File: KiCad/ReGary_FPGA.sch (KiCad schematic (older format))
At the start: 28 parts, among them J1 Conn_01x02, U1 GW1N-UV1P5LQ100, U2 LM1117-3.3, U3 TPS73643DBV

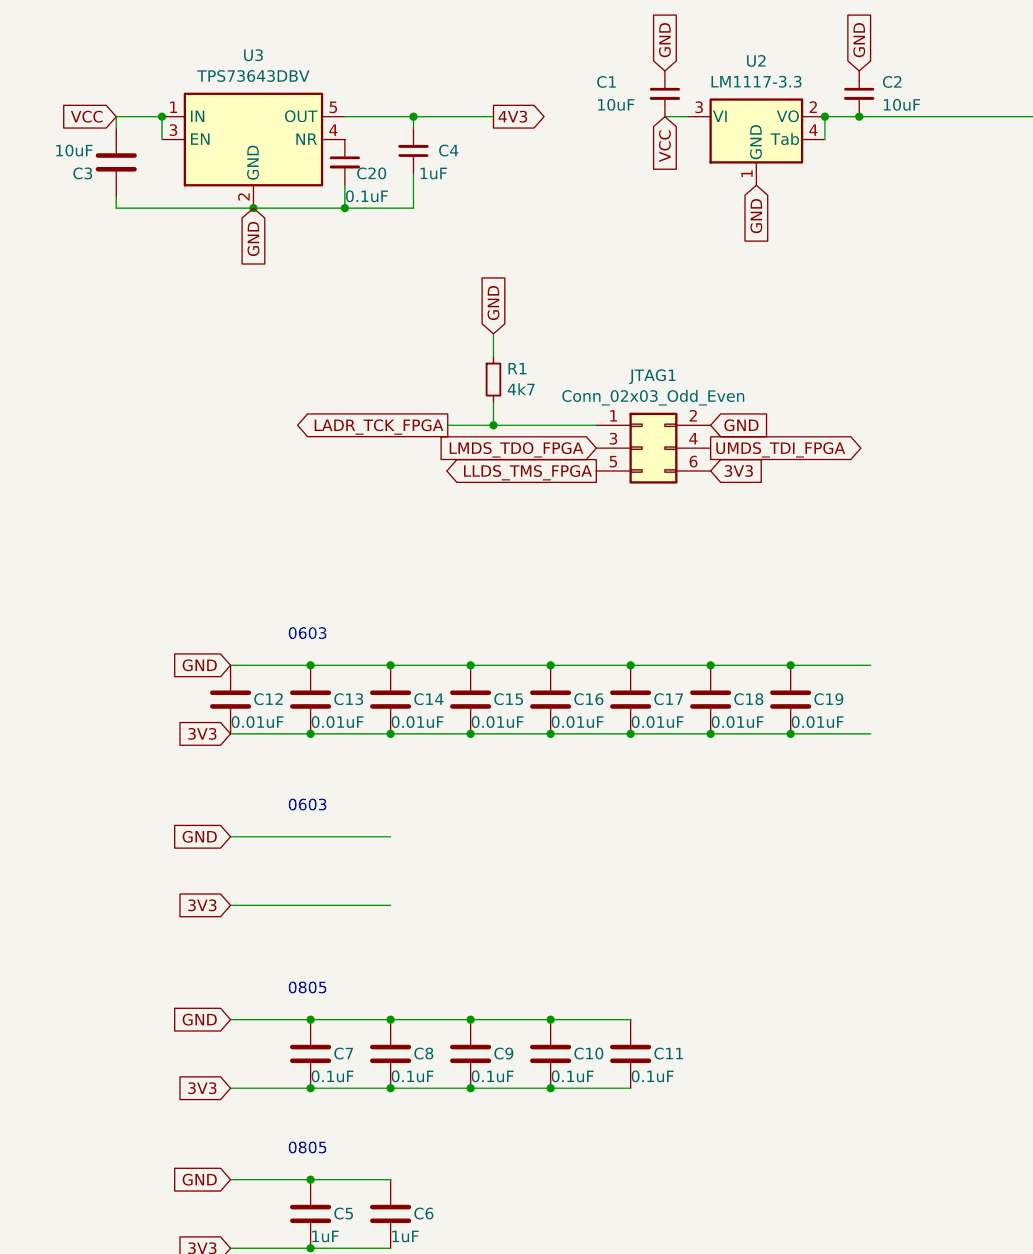
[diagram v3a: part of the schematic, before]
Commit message: Fixed enumeration of capacitors and placement of last capacitor C11 for 3V3-power
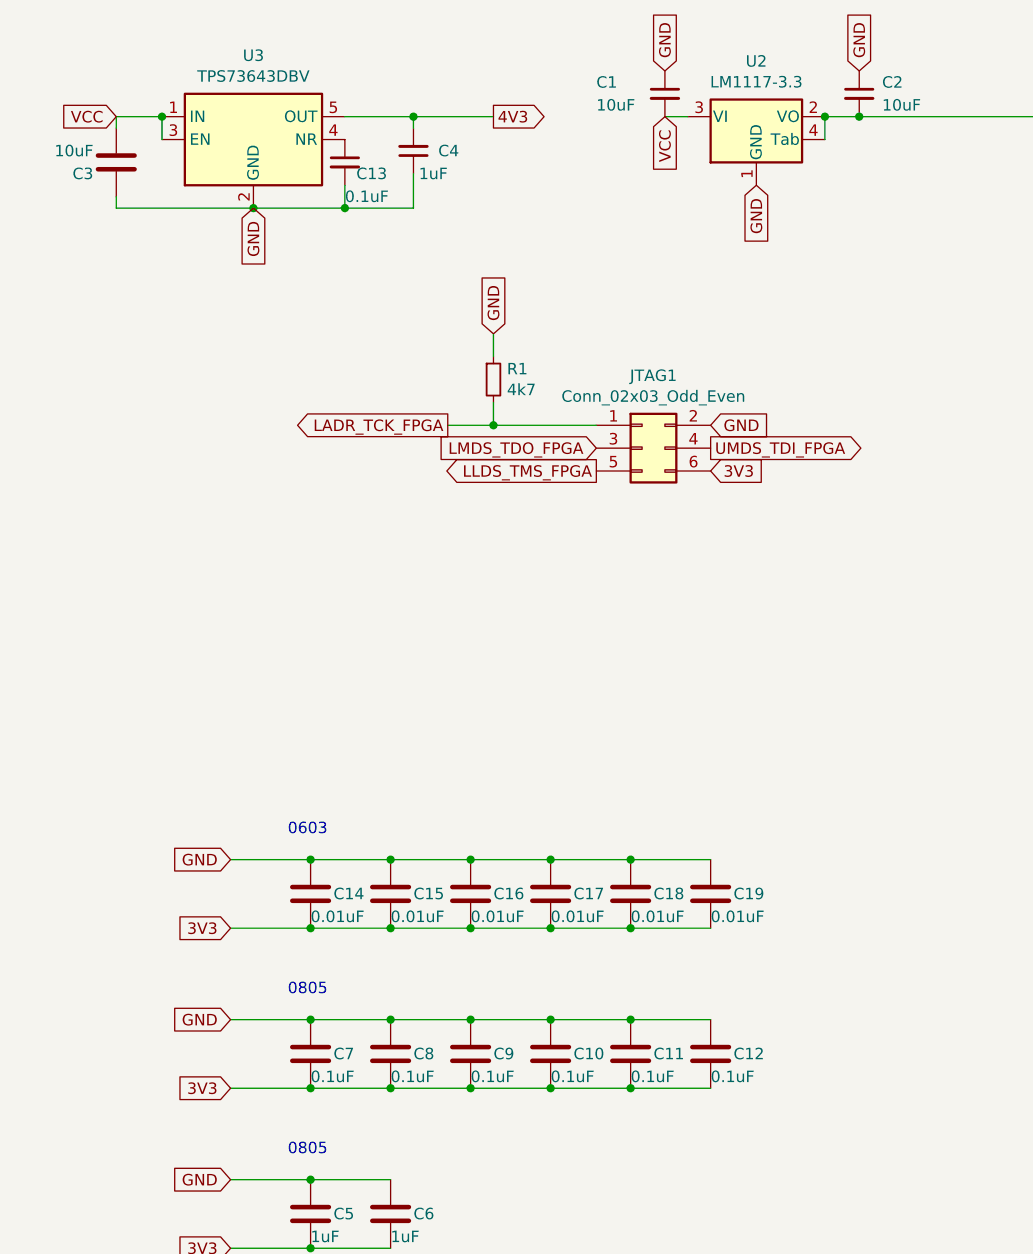
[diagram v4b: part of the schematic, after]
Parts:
- removed C19: 0.01uF, Capacitor_SMD:C_0603_1608Metric_Pad1.08x0.95mm_HandSolder, symbol Device:C
- C11: renamed from C18; value 0.01uF -> 0.1uF; footprint Capacitor_SMD:C_0603_1608Metric_Pad1.08x0.95mm_HandSolder -> Capacitor_SMD:C_0805_2012Metric_Pad1.18x1.45mm_HandSolder
- renumbered C11 to C12, C20 to C13, C12 to C14, C13 to C15, C14 to C16, C15 to C17, C16 to C18, C17 to C19
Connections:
- wire segments 78 -> 74
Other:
- moved on the sheet: C11, C12, C14, C15, C16, C17, C18, C19
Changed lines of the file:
@@
 Text GLabel 8400 2150 1    50   Input ~ 0
 GND
-Text GLabel 7250 3600 0    50   Input ~ 0
-GND
-$Comp
-L Device:C C?
-U 1 1 60CC8EFC
-P 9700 3750
-AR Path="/60CC8EFC" Ref="C?"  Part="1"
-AR Path="/608A10F5/60CC8EFC" Ref="C19"  Part="1"
-F 0 "C19" H 9800 3750 50  0000 L CNN
-F 1 "0.01uF" H 9700 3650 50  0000 L CNN
-F 2 "Capacitor_SMD:C_0603_1608Metric_Pad1.08x0.95mm_HandSolder" H 9738 3600 50  0001 C CNN
-F 3 "~" H 9700 3750 50  0001 C CNN
-	1    9700 3750
-	1    0    0    -1
-$EndComp
+Text GLabel 7250 4450 0    50   Input ~ 0
+GND
 $Comp
 L Device:C C?
 U 1 1 60CC8F02
-P 9350 3750
+P 9000 5300
 AR Path="/60CC8F02" Ref="C?"  Part="1"
-AR Path="/608A10F5/60CC8F02" Ref="C18"  Part="1"
-F 0 "C18" H 9450 3750 50  0000 L CNN
-F 1 "0.01uF" H 9350 3650 50  0000 L CNN
-F 2 "Capacitor_SMD:C_0603_1608Metric_Pad1.08x0.95mm_HandSolder" H 9388 3600 50  0001 C CNN
-F 3 "~" H 9350 3750 50  0001 C CNN
-	1    9350 3750
-	1    0    0    -1
-$EndComp
-Connection ~ 7600 3600
-Wire Wire Line
-	7600 3600 7950 3600
-Connection ~ 7600 3900
-Wire Wire Line
-	7600 3900 7950 3900
+AR Path="/608A10F5/60CC8F02" Ref="C11"  Part="1"
+F 0 "C11" H 9100 5300 50  0000 L CNN
+F 1 "0.1uF" H 9000 5200 50  0000 L CNN
+F 2 "Capacitor_SMD:C_0805_2012Metric_Pad1.18x1.45mm_HandSolder" H 9038 5150 50  0001 C CNN
+F 3 "~" H 9000 5300 50  0001 C CNN
+	1    9000 5300
+	1    0    0    -1
+$EndComp
+Connection ~ 7600 4450
+Wire Wire Line
+	7600 4450 7950 4450
+Connection ~ 7600 4750
+Wire Wire Line
+	7600 4750 7950 4750
 $Comp
 L Device:C C?
@@
 	1    0    0    -1
 $EndComp
-Connection ~ 7950 3600
-Connection ~ 7950 3900
-Wire Wire Line
-	7950 3600 8300 3600
-Wire Wire Line
-	7950 3900 8300 3900
+Connection ~ 7950 4450
+Connection ~ 7950 4750
+Wire Wire Line
+	7950 4450 8300 4450
+Wire Wire Line
+	7950 4750 8300 4750
 Text GLabel 7250 5450 0    50   Input ~ 0
 3V3
-Connection ~ 8300 3600
-Wire Wire Line
-	9000 3900 9350 3900
+Connection ~ 8300 4450
+Wire Wire Line
+	9000 4750 9350 4750
 $Comp
 L Device:C C?
@@
 	1    0    0    -1
 $EndComp
-Wire Wire Line
-	9700 3900 9350 3900
-Connection ~ 9350 3900
 $Comp
 L Device:R_Pack04 RN1
@@
 L Device:C C?
 U 1 1 60636E2E
-P 7250 3750
+P 7600 4600
 AR Path="/60636E2E" Ref="C?"  Part="1"
-AR Path="/608A10F5/60636E2E" Ref="C12"  Part="1"
-F 0 "C12" H 7350 3750 50  0000 L CNN
-F 1 "0.01uF" H 7250 3650 50  0000 L CNN
-F 2 "Capacitor_SMD:C_0603_1608Metric_Pad1.08x0.95mm_HandSolder" H 7288 3600 50  0001 C CNN
-F 3 "~" H 7250 3750 50  0001 C CNN
-	1    7250 3750
+AR Path="/608A10F5/60636E2E" Ref="C14"  Part="1"
+F 0 "C14" H 7700 4600 50  0000 L CNN
+F 1 "0.01uF" H 7600 4500 50  0000 L CNN
+F 2 "Capacitor_SMD:C_0603_1608Metric_Pad1.08x0.95mm_HandSolder" H 7638 4450 50  0001 C CNN
+F 3 "~" H 7600 4600 50  0001 C CNN
+	1    7600 4600
 	1    0    0    -1
 $EndComp
@@
 L Device:C C?
 U 1 1 60637476
-P 7600 3750
+P 7950 4600
 AR Path="/60637476" Ref="C?"  Part="1"
-AR Path="/608A10F5/60637476" Ref="C13"  Part="1"
-F 0 "C13" H 7700 3750 50  0000 L CNN
-F 1 "0.01uF" H 7600 3650 50  0000 L CNN
-F 2 "Capacitor_SMD:C_0603_1608Metric_Pad1.08x0.95mm_HandSolder" H 7638 3600 50  0001 C CNN
-F 3 "~" H 7600 3750 50  0001 C CNN
-	1    7600 3750
+AR Path="/608A10F5/60637476" Ref="C15"  Part="1"
+F 0 "C15" H 8050 4600 50  0000 L CNN
+F 1 "0.01uF" H 7950 4500 50  0000 L CNN
+F 2 "Capacitor_SMD:C_0603_1608Metric_Pad1.08x0.95mm_HandSolder" H 7988 4450 50  0001 C CNN
+F 3 "~" H 7950 4600 50  0001 C CNN
+	1    7950 4600
 	1    0    0    -1
 $EndComp
@@
 L Device:C C?
 U 1 1 60637B30
-P 8300 3750
+P 8650 4600
 AR Path="/60637B30" Ref="C?"  Part="1"
-AR Path="/608A10F5/60637B30" Ref="C15"  Part="1"
-F 0 "C15" H 8400 3750 50  0000 L CNN
-F 1 "0.01uF" H 8300 3650 50  0000 L CNN
-F 2 "Capacitor_SMD:C_0603_1608Metric_Pad1.08x0.95mm_HandSolder" H 8338 3600 50  0001 C CNN
-F 3 "~" H 8300 3750 50  0001 C CNN
-	1    8300 3750
+AR Path="/608A10F5/60637B30" Ref="C17"  Part="1"
+F 0 "C17" H 8750 4600 50  0000 L CNN
+F 1 "0.01uF" H 8650 4500 50  0000 L CNN
+F 2 "Capacitor_SMD:C_0603_1608Metric_Pad1.08x0.95mm_HandSolder" H 8688 4450 50  0001 C CNN
+F 3 "~" H 8650 4600 50  0001 C CNN
+	1    8650 4600
 	1    0    0    -1
 $EndComp
@@
 L Device:C C?
 U 1 1 60638427
-P 8650 3750
+P 9000 4600
 AR Path="/60638427" Ref="C?"  Part="1"
-AR Path="/608A10F5/60638427" Ref="C16"  Part="1"
-F 0 "C16" H 8750 3750 50  0000 L CNN
-F 1 "0.01uF" H 8650 3650 50  0000 L CNN
-F 2 "Capacitor_SMD:C_0603_1608Metric_Pad1.08x0.95mm_HandSolder" H 8688 3600 50  0001 C CNN
-F 3 "~" H 8650 3750 50  0001 C CNN
-	1    8650 3750
-	1    0    0    -1
-$EndComp
-Wire Wire Line
-	9700 3900 10050 3900
-Connection ~ 9700 3900
-Wire Wire Line
-	7250 3900 7600 3900
-Wire Wire Line
-	7250 3600 7600 3600
+AR Path="/608A10F5/60638427" Ref="C18"  Part="1"
+F 0 "C18" H 9100 4600 50  0000 L CNN
+F 1 "0.01uF" H 9000 4500 50  0000 L CNN
+F 2 "Capacitor_SMD:C_0603_1608Metric_Pad1.08x0.95mm_HandSolder" H 9038 4450 50  0001 C CNN
+F 3 "~" H 9000 4600 50  0001 C CNN
+	1    9000 4600
+	1    0    0    -1
+$EndComp
+Wire Wire Line
+	7250 4750 7600 4750
+Wire Wire Line
+	7250 4450 7600 4450
 Text GLabel 7250 5150 0    50   Input ~ 0
 GND
-Text GLabel 7250 3900 0    50   Input ~ 0
-3V3
-Text Notes 7500 3500 0    50   ~ 0
+Text GLabel 7250 4750 0    50   Input ~ 0
+3V3
+Text Notes 7500 4350 0    50   ~ 0
 0603
 Text Notes 7500 5050 0    50   ~ 0
@@
 L Device:C C?
 U 1 1 60898D1D
-P 9000 3750
+P 9350 4600
 AR Path="/60898D1D" Ref="C?"  Part="1"
-AR Path="/608A10F5/60898D1D" Ref="C17"  Part="1"
-F 0 "C17" H 9100 3750 50  0000 L CNN
-F 1 "0.01uF" H 9000 3650 50  0000 L CNN
-F 2 "Capacitor_SMD:C_0603_1608Metric_Pad1.08x0.95mm_HandSolder" H 9038 3600 50  0001 C CNN
-F 3 "~" H 9000 3750 50  0001 C CNN
-	1    9000 3750
-	1    0    0    -1
-$EndComp
-Wire Wire Line
-	9350 3600 9700 3600
-Connection ~ 9350 3600
-Wire Wire Line
-	8300 3600 8650 3600
-Connection ~ 8650 3600
-Wire Wire Line
-	8650 3600 9000 3600
+AR Path="/608A10F5/60898D1D" Ref="C19"  Part="1"
+F 0 "C19" H 9450 4600 50  0000 L CNN
+F 1 "0.01uF" H 9350 4500 50  0000 L CNN
+F 2 "Capacitor_SMD:C_0603_1608Metric_Pad1.08x0.95mm_HandSolder" H 9388 4450 50  0001 C CNN
+F 3 "~" H 9350 4600 50  0001 C CNN
+	1    9350 4600
+	1    0    0    -1
+$EndComp
+Wire Wire Line
+	8300 4450 8650 4450
+Connection ~ 8650 4450
+Wire Wire Line
+	8650 4450 9000 4450
 $Comp
 L Device:C C?
 U 1 1 608A7236
-P 7950 3750
+P 8300 4600
 AR Path="/608A7236" Ref="C?"  Part="1"
-AR Path="/608A10F5/608A7236" Ref="C14"  Part="1"
-F 0 "C14" H 8050 3750 50  0000 L CNN
-F 1 "0.01uF" H 7950 3650 50  0000 L CNN
-F 2 "Capacitor_SMD:C_0603_1608Metric_Pad1.08x0.95mm_HandSolder" H 7988 3600 50  0001 C CNN
-F 3 "~" H 7950 3750 50  0001 C CNN
-	1    7950 3750
-	1    0    0    -1
-$EndComp
-Connection ~ 9000 3600
-Wire Wire Line
-	9000 3600 9350 3600
-Wire Wire Line
-	10050 3600 9700 3600
-Connection ~ 9700 3600
-Wire Wire Line
-	8300 3900 8650 3900
-Connection ~ 8300 3900
-Connection ~ 9000 3900
-Connection ~ 8650 3900
-Wire Wire Line
-	8650 3900 9000 3900
+AR Path="/608A10F5/608A7236" Ref="C16"  Part="1"
+F 0 "C16" H 8400 4600 50  0000 L CNN
+F 1 "0.01uF" H 8300 4500 50  0000 L CNN
+F 2 "Capacitor_SMD:C_0603_1608Metric_Pad1.08x0.95mm_HandSolder" H 8338 4450 50  0001 C CNN
+F 3 "~" H 8300 4600 50  0001 C CNN
+	1    8300 4600
+	1    0    0    -1
+$EndComp
+Connection ~ 9000 4450
+Wire Wire Line
+	9000 4450 9350 4450
+Wire Wire Line
+	8300 4750 8650 4750
+Connection ~ 8300 4750
+Connection ~ 9000 4750
+Connection ~ 8650 4750
+Wire Wire Line
+	8650 4750 9000 4750
 $Comp
 L Device:C C?
@@
 L Device:C C?
 U 1 1 6084459F
-P 9000 5300
+P 9350 5300
 AR Path="/6084459F" Ref="C?"  Part="1"
-AR Path="/608A10F5/6084459F" Ref="C11"  Part="1"
-F 0 "C11" H 9100 5300 50  0000 L CNN
-F 1 "0.1uF" H 9000 5200 50  0000 L CNN
-F 2 "Capacitor_SMD:C_0805_2012Metric_Pad1.18x1.45mm_HandSolder" H 9038 5150 50  0001 C CNN
-F 3 "~" H 9000 5300 50  0001 C CNN
-	1    9000 5300
+AR Path="/608A10F5/6084459F" Ref="C12"  Part="1"
+F 0 "C12" H 9450 5300 50  0000 L CNN
+F 1 "0.1uF" H 9350 5200 50  0000 L CNN
+F 2 "Capacitor_SMD:C_0805_2012Metric_Pad1.18x1.45mm_HandSolder" H 9388 5150 50  0001 C CNN
+F 3 "~" H 9350 5300 50  0001 C CNN
+	1    9350 5300
 	1    0    0    -1
 $EndComp
@@
 P 7750 1400
 AR Path="/60785965" Ref="C?"  Part="1"
-AR Path="/608A10F5/60785965" Ref="C20"  Part="1"
-F 0 "C20" H 7800 1350 50  0000 L CNN
+AR Path="/608A10F5/60785965" Ref="C13"  Part="1"
+F 0 "C13" H 7800 1350 50  0000 L CNN
 F 1 "0.1uF" H 7750 1250 50  0000 L CNN
 F 2 "Capacitor_SMD:C_0603_1608Metric_Pad1.08x0.95mm_HandSolder" H 7788 1250 50  0001 C CNN
@@
 Wire Wire Line
 	7750 1600 8050 1600
-Text GLabel 7250 4650 0    50   Input ~ 0
-3V3
-Text GLabel 7250 4350 0    50   Input ~ 0
-GND
-Text Notes 7500 4250 0    50   ~ 0
-0603
-Wire Wire Line
-	7250 4350 7950 4350
-Wire Wire Line
-	7250 4650 7950 4650
 $Comp
 L Device:C C?
@@
 Wire Wire Line
 	2500 6200 2500 6850
+Wire Wire Line
+	9000 5150 9350 5150
+Connection ~ 9000 5150
+Wire Wire Line
+	9000 5450 9350 5450
+Connection ~ 9000 5450
 $EndSCHEMATC

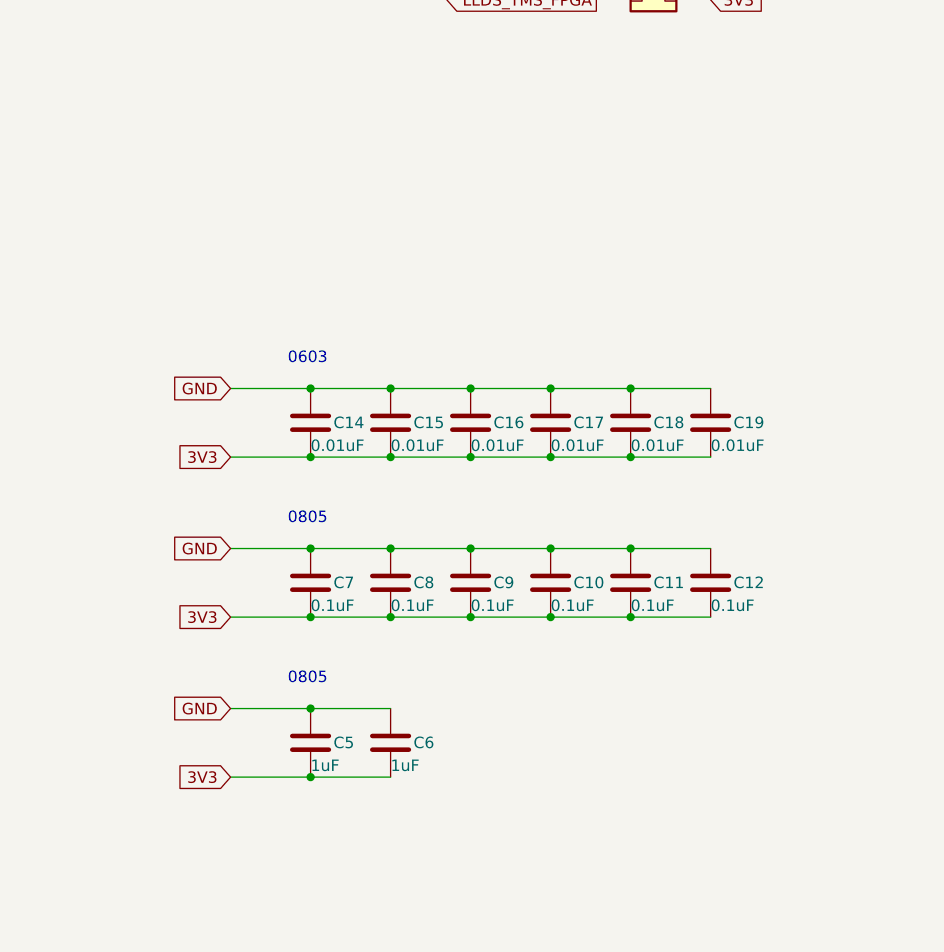
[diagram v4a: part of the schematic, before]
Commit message: Fixed JTAGSEL_N header size and silkscreen placement
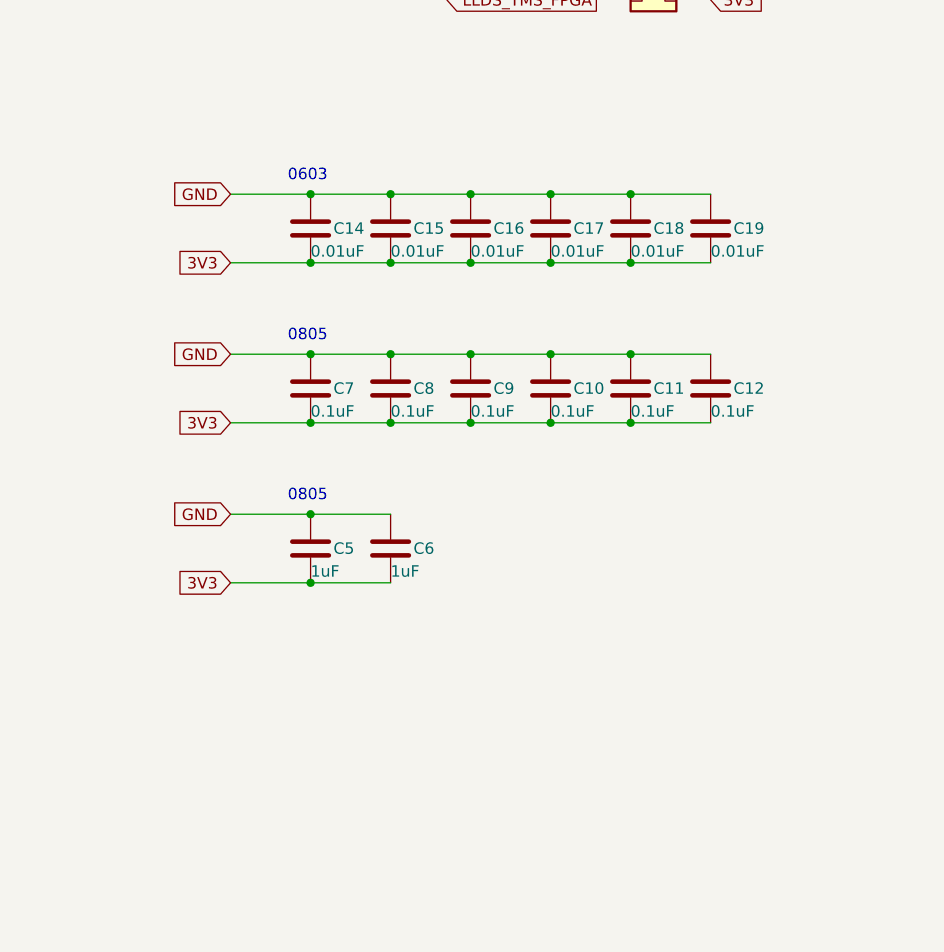
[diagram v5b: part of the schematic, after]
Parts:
- J1: footprint Connector_PinHeader_2.00mm:PinHeader_1x02_P2.00mm_Vertical -> Connector_PinHeader_2.54mm:PinHeader_1x02_P2.54mm_Vertical
- renumbered C15 to C14, C14 to C15
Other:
- moved on the sheet: C10, C11, C12, C14, C15, C16, C17, C18, C19, C5, C6, C7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
